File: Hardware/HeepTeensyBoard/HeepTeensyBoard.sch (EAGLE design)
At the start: 25 parts, among them J1 MAGJACK, Q1 25MHz, U1 ENC28J60-SO

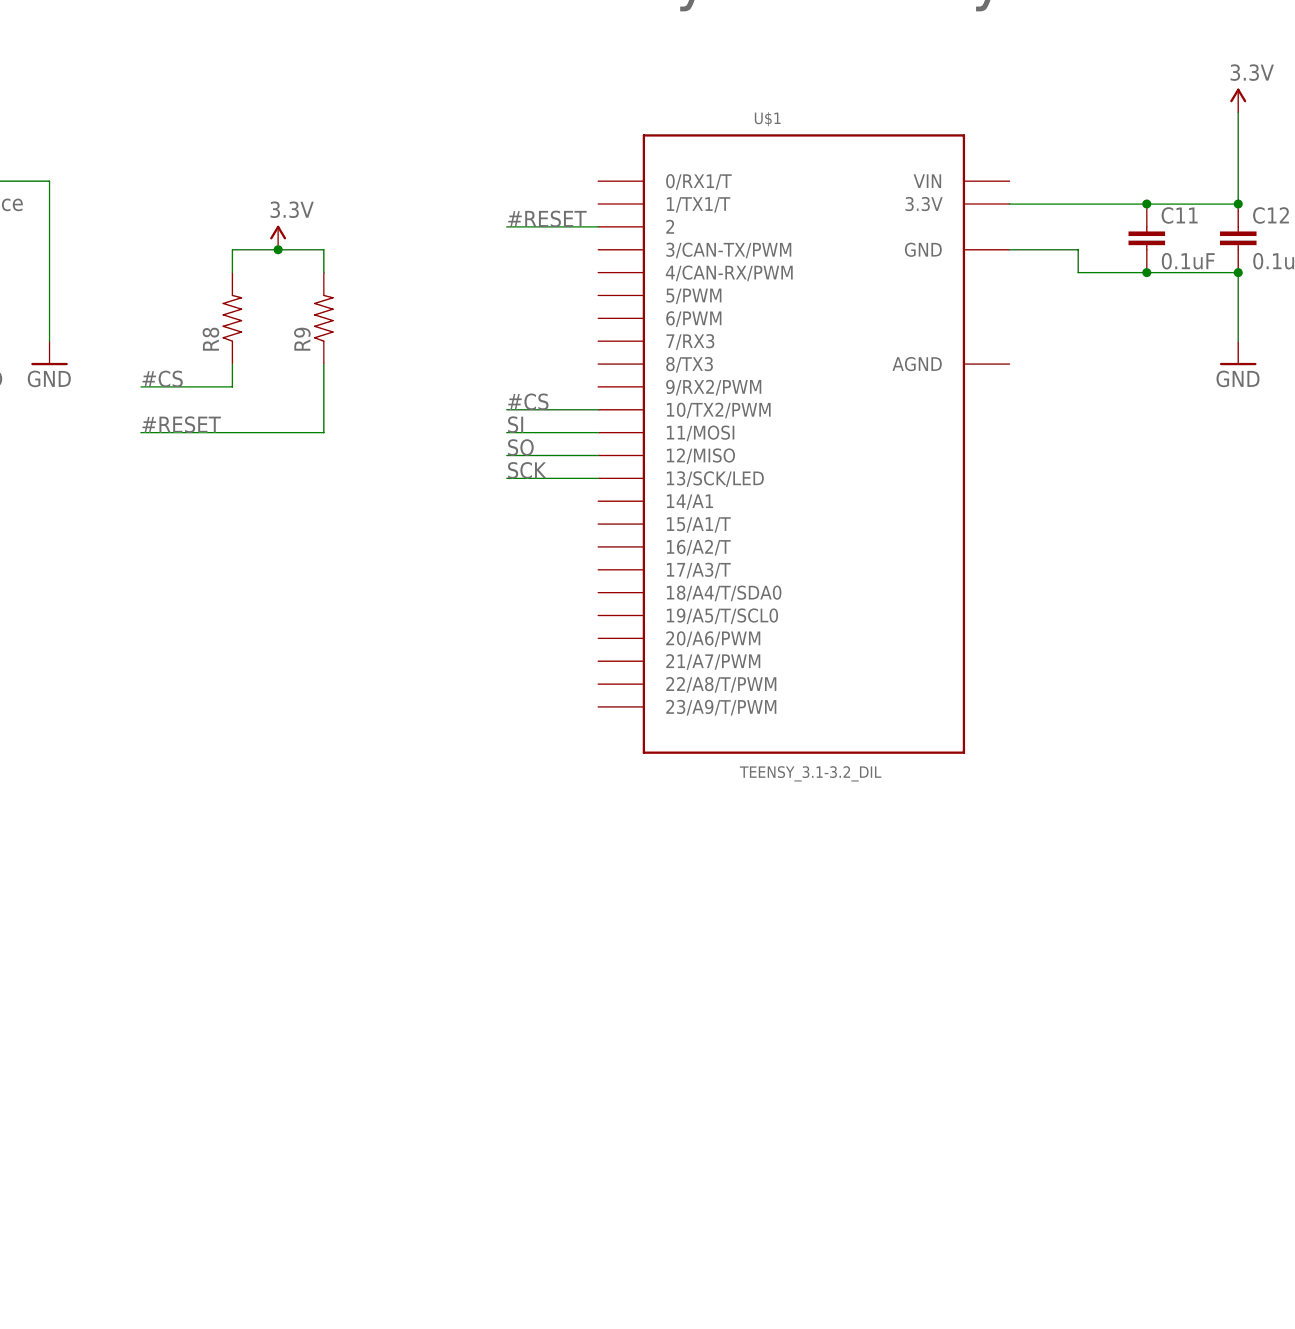
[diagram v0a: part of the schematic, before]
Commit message: Added header sockets
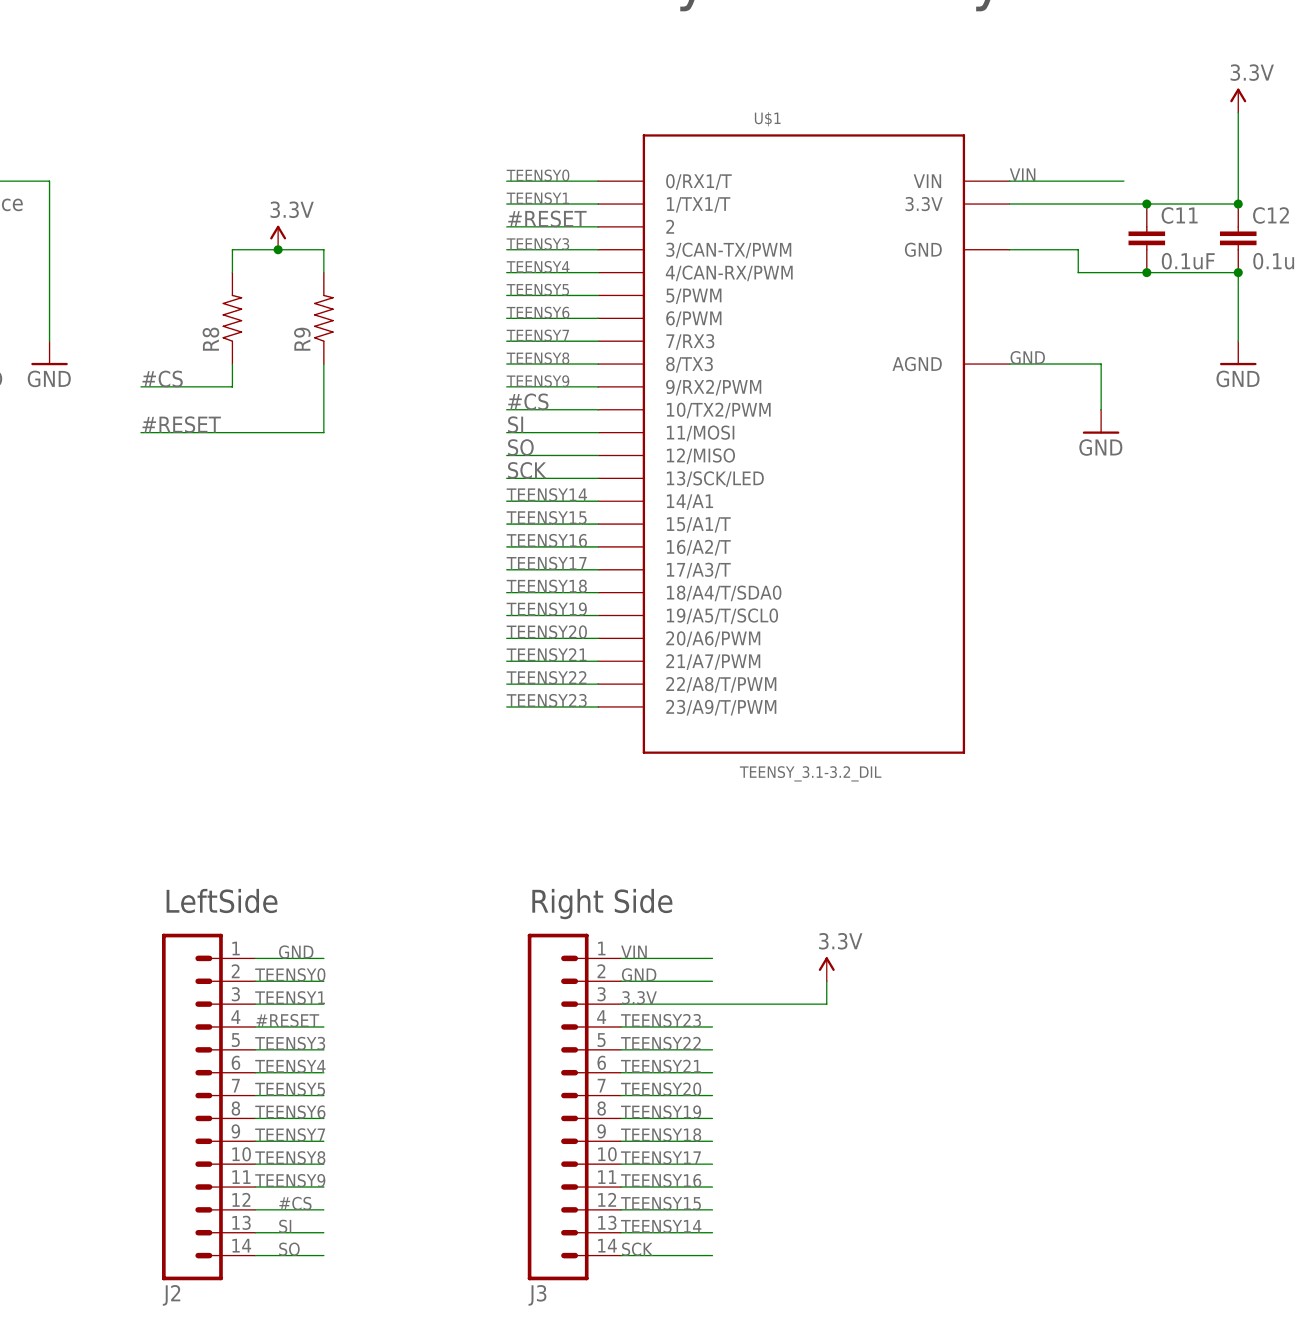
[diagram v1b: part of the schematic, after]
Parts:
- added J2, J3: (no value), SparkFun-Connectors:M14
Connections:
- new net TEENSY0: J2.2, U$1.0/RX1/T
- new net TEENSY1: J2.3, U$1.1/TX1/T
- new net TEENSY14: J3.13, U$1.14/A1
- new net TEENSY15: J3.12, U$1.15/A1/T
- new net TEENSY16: J3.11, U$1.16/A2/T
- new net TEENSY17: J3.10, U$1.17/A3/T
- new net TEENSY18: J3.9, U$1.18/A4/T/SDA0
- new net TEENSY19: J3.8, U$1.19/A5/T/SCL0
- new net TEENSY20: J3.7, U$1.20/A6/PWM
- new net TEENSY21: J3.6, U$1.21/A7/PWM
- new net TEENSY22: J3.5, U$1.22/A8/T/PWM
- new net TEENSY23: J3.4, U$1.23/A9/T/PWM
- new net TEENSY3: J2.5, U$1.3/CAN-TX/PWM
- new net TEENSY4: J2.6, U$1.4/CAN-RX/PWM
- new net TEENSY5: J2.7, U$1.5/PWM
- new net TEENSY6: J2.8, U$1.6/PWM
- new net TEENSY7: J2.9, U$1.7/RX3
- new net TEENSY8: J2.10, U$1.8/TX3
- new net TEENSY9: J2.11, U$1.9/RX2/PWM
- new net VIN: J3.1, U$1.VIN
- net #CS: now also J2.12
- net #RESET: now also J2.4
- net 3.3V: now also J3.3
- net GND: now also J2.1, J3.2, U$1.AGND
- net SCK: now also J3.14
- net SI: now also J2.13
- net SO: now also J2.14
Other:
- note added: "LeftSide"
- note added: "Right Side"

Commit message: #151 Added the circuit board file
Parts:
- added D1: RED, SparkFun-LED:LED-RED0603
- added R10: 200, SparkFun-Passives:RESISTOR0603-RES
- R8, R9: value (none) -> 10k
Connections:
- new net N$8: D1.A, R10.1
- net 3.3V: now also R10.2
- net GND: now also D1.C
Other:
- note added: "Power LED"
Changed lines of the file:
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@@
 <part name="GND8" library="SparkFun-Aesthetics" deviceset="GND" device=""/>
 <part name="GND9" library="SparkFun-Aesthetics" deviceset="GND" device=""/>
-<part name="R8" library="SparkFun-Passives" deviceset="RESISTOR" device="0603-RES"/>
-<part name="R9" library="SparkFun-Passives" deviceset="RESISTOR" device="0603-RES"/>
+<part name="R8" library="SparkFun-Passives" deviceset="RESISTOR" device="0603-RES" value="10k"/>
+<part name="R9" library="SparkFun-Passives" deviceset="RESISTOR" device="0603-RES" value="10k"/>
 <part name="SUPPLY2" library="SparkFun-Aesthetics" deviceset="3.3V" device=""/>
 <part name="C11" library="SparkFun-Capacitors" deviceset="CAP" device="0603-CAP" value="0.1uF"/>
@@
 <part name="SUPPLY4" library="SparkFun-Aesthetics" deviceset="3.3V" device=""/>
 <part name="GND11" library="SparkFun-Aesthetics" deviceset="GND" device=""/>
+<part name="D1" library="SparkFun-LED" deviceset="LED-RED" device="0603" value="RED"/>
+<part name="R10" library="SparkFun-Passives" deviceset="RESISTOR" device="0603-RES" value="200"/>
+<part name="SUPPLY5" library="SparkFun-Aesthetics" deviceset="3.3V" device=""/>
+<part name="GND12" library="SparkFun-Aesthetics" deviceset="GND" device=""/>
 </parts>
 <sheets>
@@
 <text x="38.1" y="7.62" size="2.54" layer="97">LeftSide</text>
 <text x="78.74" y="7.62" size="2.54" layer="97">Right Side</text>
+<text x="175.26" y="111.76" size="2.54" layer="97">Power LED</text>
 </plain>
 <instances>
@@
 <instance part="SUPPLY4" gate="G$1" x="111.76" y="0"/>
 <instance part="GND11" gate="1" x="142.24" y="60.96"/>
+<instance part="D1" gate="G$1" x="182.88" y="83.82"/>
+<instance part="R10" gate="G$1" x="182.88" y="93.98" rot="R90"/>
+<instance part="SUPPLY5" gate="G$1" x="182.88" y="104.14"/>
+<instance part="GND12" gate="1" x="182.88" y="71.12"/>
 </instances>
 <busses>
@@
 <wire x1="88.9" y1="0" x2="99.06" y2="0" width="0.1524" layer="91"/>
 <label x="88.9" y="0" size="1.4224" layer="95"/>
+</segment>
+<segment>
+<pinref part="D1" gate="G$1" pin="C"/>
+<wire x1="182.88" y1="78.74" x2="182.88" y2="73.66" width="0.1524" layer="91"/>
+<pinref part="GND12" gate="1" pin="GND"/>
 </segment>
 </net>
@@
 <label x="88.9" y="-2.54" size="1.4224" layer="95"/>
 </segment>
+<segment>
+<pinref part="R10" gate="G$1" pin="2"/>
+<wire x1="182.88" y1="99.06" x2="182.88" y2="104.14" width="0.1524" layer="91"/>
+<pinref part="SUPPLY5" gate="G$1" pin="3.3V"/>
+</segment>
 </net>
 <net name="N$15" class="0">
@@
 </segment>
 </net>
+<net name="N$8" class="0">
+<segment>
+<pinref part="R10" gate="G$1" pin="1"/>
+<pinref part="D1" gate="G$1" pin="A"/>
+<wire x1="182.88" y1="88.9" x2="182.88" y2="86.36" width="0.1524" layer="91"/>
+</segment>
+</net>

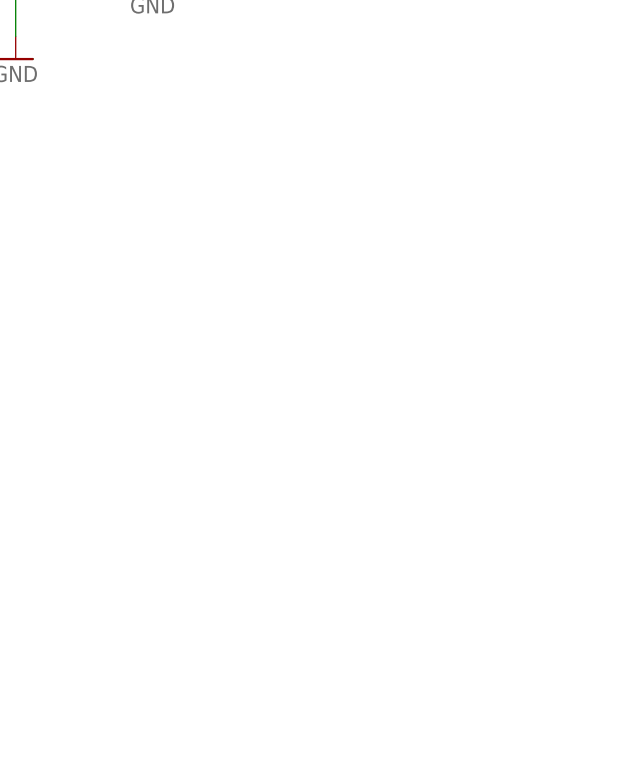
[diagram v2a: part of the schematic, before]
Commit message: Added power inputs
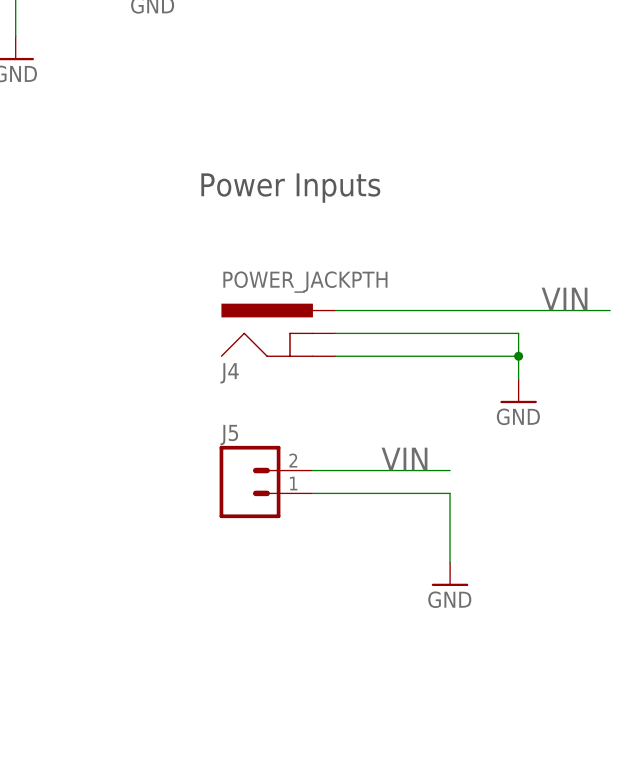
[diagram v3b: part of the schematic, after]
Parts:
- added J4: POWER_JACKPTH, SparkFun-Connectors:POWER_JACKPTH
- added J5: (no value), SparkFun-Connectors:M02PTH
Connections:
- net GND: now also J4.GND, J4.GNDBREAK, J5.1
- net VIN: now also J4.PWR, J5.2
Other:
- note added: "Power Inputs"
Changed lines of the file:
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@@
 <part name="SUPPLY5" library="SparkFun-Aesthetics" deviceset="3.3V" device=""/>
 <part name="GND12" library="SparkFun-Aesthetics" deviceset="GND" device=""/>
+<part name="J4" library="SparkFun-Connectors" deviceset="POWER_JACK" device="PTH"/>
+<part name="GND13" library="SparkFun-Aesthetics" deviceset="GND" device=""/>
+<part name="J5" library="SparkFun-Connectors" deviceset="M02" device="PTH"/>
+<part name="GND14" library="SparkFun-Aesthetics" deviceset="GND" device=""/>
 </parts>
 <sheets>
@@
 <text x="78.74" y="7.62" size="2.54" layer="97">Right Side</text>
 <text x="175.26" y="111.76" size="2.54" layer="97">Power LED</text>
+<text x="162.56" y="45.72" size="2.54" layer="97">Power Inputs</text>
 </plain>
 <instances>
@@
 <instance part="SUPPLY5" gate="G$1" x="182.88" y="104.14"/>
 <instance part="GND12" gate="1" x="182.88" y="71.12"/>
+<instance part="J4" gate="G$1" x="175.26" y="25.4"/>
+<instance part="GND13" gate="1" x="198.12" y="22.86"/>
+<instance part="J5" gate="G$1" x="167.64" y="12.7"/>
+<instance part="GND14" gate="1" x="190.5" y="2.54"/>
 </instances>
 <busses>
@@
 <wire x1="182.88" y1="78.74" x2="182.88" y2="73.66" width="0.1524" layer="91"/>
 <pinref part="GND12" gate="1" pin="GND"/>
+</segment>
+<segment>
+<pinref part="J4" gate="G$1" pin="GNDBREAK"/>
+<wire x1="177.8" y1="30.48" x2="198.12" y2="30.48" width="0.1524" layer="91"/>
+<wire x1="198.12" y1="30.48" x2="198.12" y2="27.94" width="0.1524" layer="91"/>
+<pinref part="J4" gate="G$1" pin="GND"/>
+<wire x1="198.12" y1="27.94" x2="198.12" y2="25.4" width="0.1524" layer="91"/>
+<wire x1="177.8" y1="27.94" x2="198.12" y2="27.94" width="0.1524" layer="91"/>
+<junction x="198.12" y="27.94"/>
+<pinref part="GND13" gate="1" pin="GND"/>
+</segment>
+<segment>
+<pinref part="J5" gate="G$1" pin="1"/>
+<wire x1="175.26" y1="12.7" x2="190.5" y2="12.7" width="0.1524" layer="91"/>
+<wire x1="190.5" y1="12.7" x2="190.5" y2="5.08" width="0.1524" layer="91"/>
+<pinref part="GND14" gate="1" pin="GND"/>
 </segment>
 </net>
@@
 <label x="88.9" y="2.54" size="1.4224" layer="95"/>
 </segment>
-</net>
+<segment>
+<pinref part="J4" gate="G$1" pin="PWR"/>
+<wire x1="177.8" y1="33.02" x2="208.28" y2="33.02" width="0.1524" layer="91"/>
+<label x="200.66" y="33.02" size="2.54" layer="95"/>
+</segment>
+<segment>
+<pinref part="J5" gate="G$1" pin="2"/>
+<wire x1="175.26" y1="15.24" x2="190.5" y2="15.24" width="0.1524" layer="91"/>
+<label x="182.88" y="15.24" size="2.54" layer="95"/>
+</segment>
+</net>

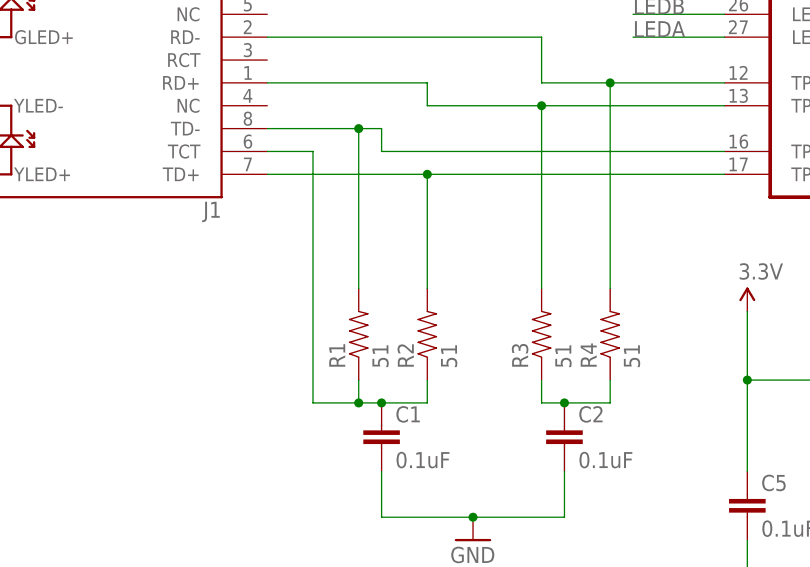
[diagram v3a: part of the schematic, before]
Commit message: #156 Added a ferrite bead to layout and schematic of pure teensy board
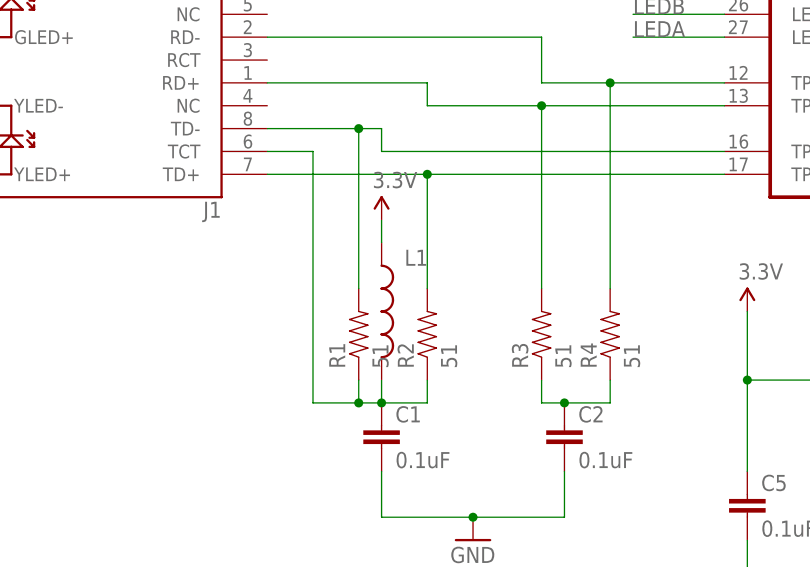
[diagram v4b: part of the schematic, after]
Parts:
- added L1: (no value), SparkFun-Passives:INDUCTOR0603
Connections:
- net 3.3V: now also L1.1
- net N$7: now also L1.2
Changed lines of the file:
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@@
 <part name="J5" library="SparkFun-Connectors" deviceset="M02" device="PTH"/>
 <part name="GND14" library="SparkFun-Aesthetics" deviceset="GND" device=""/>
+<part name="L1" library="SparkFun-Passives" deviceset="INDUCTOR" device="0603"/>
+<part name="SUPPLY6" library="SparkFun-Aesthetics" deviceset="3.3V" device=""/>
 </parts>
 <sheets>
@@
 <instance part="J5" gate="G$1" x="167.64" y="12.7"/>
 <instance part="GND14" gate="1" x="190.5" y="2.54"/>
+<instance part="L1" gate="G$1" x="-96.52" y="35.56"/>
+<instance part="SUPPLY6" gate="G$1" x="-96.52" y="45.72"/>
 </instances>
 <busses>
@@
 <wire x1="-104.14" y1="25.4" x2="-99.06" y2="25.4" width="0.1524" layer="91"/>
 <junction x="-99.06" y="25.4"/>
+<pinref part="L1" gate="G$1" pin="2"/>
+<wire x1="-96.52" y1="27.94" x2="-96.52" y2="25.4" width="0.1524" layer="91"/>
 </segment>
 </net>
@@
 <pinref part="SUPPLY5" gate="G$1" pin="3.3V"/>
 </segment>
-</net>
+<segment>
+<pinref part="L1" gate="G$1" pin="1"/>
+<pinref part="SUPPLY6" gate="G$1" pin="3.3V"/>
+<wire x1="-96.52" y1="43.18" x2="-96.52" y2="45.72" width="0.1524" layer="91"/>
+</segment>
+</net>
